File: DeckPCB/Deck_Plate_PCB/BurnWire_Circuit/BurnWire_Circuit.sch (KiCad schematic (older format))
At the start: 8 parts, among them J1 Board_to_Board, Q1 BurnWire

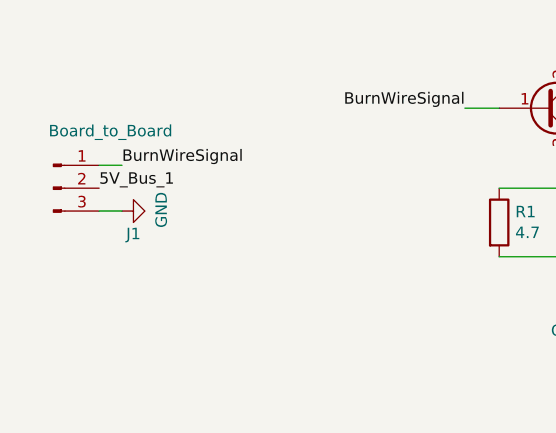
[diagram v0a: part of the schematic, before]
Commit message: updated PCB routing and creation of BurnWire circuit board and updated Daughter_Board
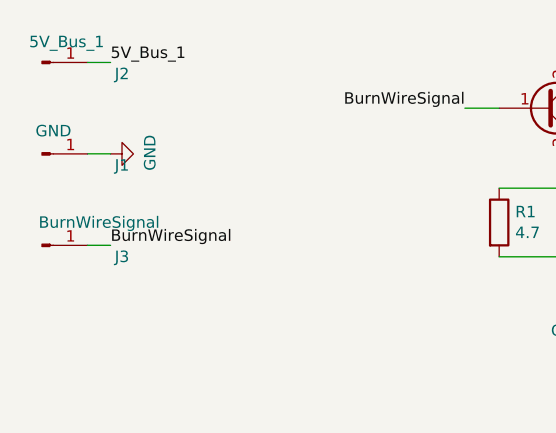
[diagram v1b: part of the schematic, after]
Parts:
- removed J1: Board_to_Board, Connector_PinHeader_2.54mm:PinHeader_1x03_P2.54mm_Vertical, symbol Connector:Conn_01x03_Male
- added J1: GND, Deck_Plate_PCB:Terminal_Lug_PCB, symbol Connector:Conn_01x01_Male
- added J2: 5V_Bus_1, Deck_Plate_PCB:Terminal_Lug_PCB, symbol Connector:Conn_01x01_Male
- added J3: BurnWireSignal, Deck_Plate_PCB:Terminal_Lug_PCB, symbol Connector:Conn_01x01_Male
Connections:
- net 5V_Bus_1: now also J2.1 (Pin_1)
- net BurnWireSignal: now also J3.1 (Pin_1)
- net GND: now also J1.1 (Pin_1)
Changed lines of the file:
@@
 Text Label 3100 2150 2    50   ~ 0
 BurnWireSignal
-$Comp
-L Connector:Conn_01x03_Male J1
-U 1 1 5E6D3E34
-P 1300 2500
-F 0 "J1" H 1650 2300 50  0000 C CNN
-F 1 "Board_to_Board" H 1550 2750 50  0000 C CNN
-F 2 "Connector_PinHeader_2.54mm:PinHeader_1x03_P2.54mm_Vertical" H 1300 2500 50  0001 C CNN
-F 3 "~" H 1300 2500 50  0001 C CNN
-	1    1300 2500
-	1    0    0    -1
-$EndComp
-Wire Wire Line
-	1500 2400 1600 2400
-Wire Wire Line
-	1500 2600 1600 2600
-Text Label 1600 2400 0    50   ~ 0
+Text Label 1550 2750 0    50   ~ 0
 BurnWireSignal
-Text Label 1500 2500 0    50   ~ 0
-5V_Bus_1
-$Comp
-L power:GND #PWR0104
-U 1 1 5E6D5ACD
-P 1600 2600
-F 0 "#PWR0104" H 1600 2350 50  0001 C CNN
-F 1 "GND" H 1605 2427 50  0000 C CNN
-F 2 "" H 1600 2600 50  0001 C CNN
-F 3 "" H 1600 2600 50  0001 C CNN
-	1    1600 2600
-	0    -1   -1   0
-$EndComp
 $Comp
 L Mechanical:MountingHole H2
@@
 	1    0    0    -1
 $EndComp
+$Comp
+L Connector:Conn_01x01_Male J2
+U 1 1 5E6393AF
+P 1250 1950
+F 0 "J2" H 1600 1900 50  0000 C CNN
+F 1 "5V_Bus_1" H 1358 2040 50  0000 C CNN
+F 2 "Deck_Plate_PCB:Terminal_Lug_PCB" H 1250 1950 50  0001 C CNN
+F 3 "~" H 1250 1950 50  0001 C CNN
+	1    1250 1950
+	1    0    0    -1
+$EndComp
+Wire Wire Line
+	1450 1950 1550 1950
+Text Label 1550 1950 0    50   ~ 0
+5V_Bus_1
+$Comp
+L Connector:Conn_01x01_Male J1
+U 1 1 5E63BC0F
+P 1250 2350
+F 0 "J1" H 1600 2300 50  0000 C CNN
+F 1 "GND" H 1300 2450 50  0000 C CNN
+F 2 "Deck_Plate_PCB:Terminal_Lug_PCB" H 1250 2350 50  0001 C CNN
+F 3 "~" H 1250 2350 50  0001 C CNN
+	1    1250 2350
+	1    0    0    -1
+$EndComp
+Wire Wire Line
+	1450 2350 1550 2350
+$Comp
+L Connector:Conn_01x01_Male J3
+U 1 1 5E63C2C1
+P 1250 2750
+F 0 "J3" H 1600 2700 50  0000 C CNN
+F 1 "BurnWireSignal" H 1500 2850 50  0000 C CNN
+F 2 "Deck_Plate_PCB:Terminal_Lug_PCB" H 1250 2750 50  0001 C CNN
+F 3 "~" H 1250 2750 50  0001 C CNN
+	1    1250 2750
+	1    0    0    -1
+$EndComp
+Wire Wire Line
+	1450 2750 1550 2750
+$Comp
+L power:GND #PWR0102
+U 1 1 5E63C41A
+P 1550 2350
+F 0 "#PWR0102" H 1550 2100 50  0001 C CNN
+F 1 "GND" H 1555 2177 50  0000 C CNN
+F 2 "" H 1550 2350 50  0001 C CNN
+F 3 "" H 1550 2350 50  0001 C CNN
+	1    1550 2350
+	0    -1   -1   0
+$EndComp
 $EndSCHEMATC

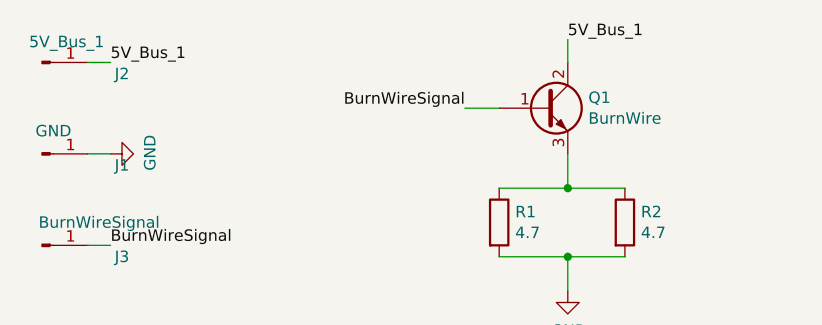
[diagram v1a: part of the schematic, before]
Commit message: Updated Main_Deck_Plate and Daughter_Board to fit Electronics Enclosure internal dimensions. Created all PCB Gerber files. Created all PCB PNG images. Created all PCB STEP files for mechanical integration. Implemented all design review comments and corrections.
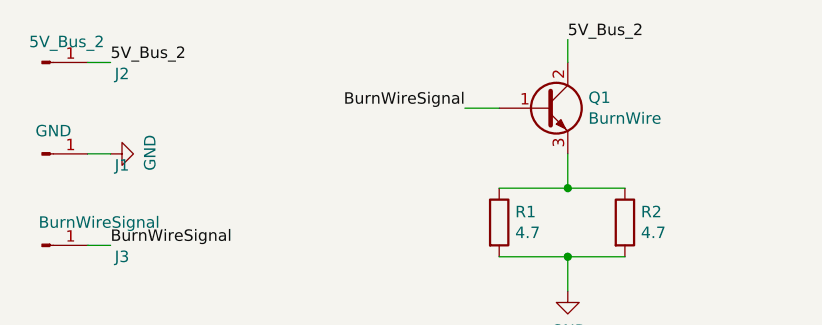
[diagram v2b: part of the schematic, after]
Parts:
- J2: value 5V_Bus_1 -> 5V_Bus_2
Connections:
- net 5V_Bus_1 renamed 5V_Bus_2
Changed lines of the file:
@@
 	3250 2800 3550 2800
 Text Label 3550 1850 0    50   ~ 0
-5V_Bus_1
+5V_Bus_2
 Text Label 3100 2150 2    50   ~ 0
 BurnWireSignal
@@
 P 1250 1950
 F 0 "J2" H 1600 1900 50  0000 C CNN
-F 1 "5V_Bus_1" H 1358 2040 50  0000 C CNN
+F 1 "5V_Bus_2" H 1358 2040 50  0000 C CNN
 F 2 "Deck_Plate_PCB:Terminal_Lug_PCB" H 1250 1950 50  0001 C CNN
 F 3 "~" H 1250 1950 50  0001 C CNN
@@
 	1450 1950 1550 1950
 Text Label 1550 1950 0    50   ~ 0
-5V_Bus_1
+5V_Bus_2
 $Comp
 L Connector:Conn_01x01_Male J1
